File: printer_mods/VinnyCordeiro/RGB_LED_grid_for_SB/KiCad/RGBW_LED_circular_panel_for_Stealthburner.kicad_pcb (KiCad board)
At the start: 2 copper layers, 13.4 x 11.6 mm, 11 parts, among them J1 Conn_02x03_Odd_Even

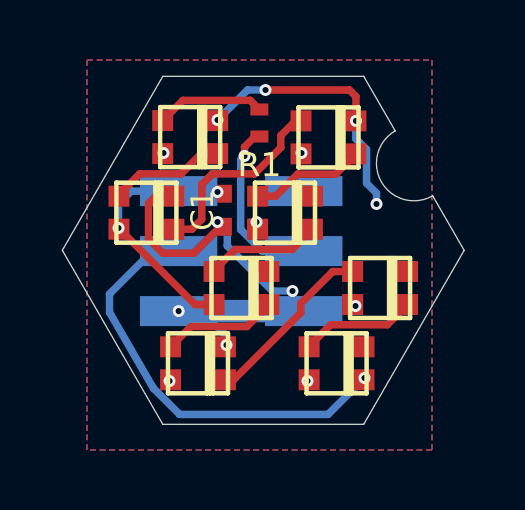
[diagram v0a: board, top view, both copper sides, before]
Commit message: Updated PCB, solve need for inline resistor for impedance matching (#716)
* Create README.md

* Create README.md

* Update README.md

* Added KiCad project files

* Create README.md

* Added production files

* Update README.md

Added note on mixing RGB and RGBW LEDs.

* Update README.md

typo

* Create README.md

* Update README.md

Added VinnyCordeiro's RGB LED grid for Stealthburner

* Add files via upload

Animated GIF of the board working

* Update README.md

* Update README.md

* Update README.md

Added the KiCad version that was used to design the PCB

* Removed non-necessary components

Removed both the input resistor and the filtering capacitor, as they are not strictly necessary for this application.

* Delete bom.csv

* Delete cpl.csv

* Delete RGBW_LED_circular_panel_for_Stealthburner.zip

* Updated production files

* Update README.md
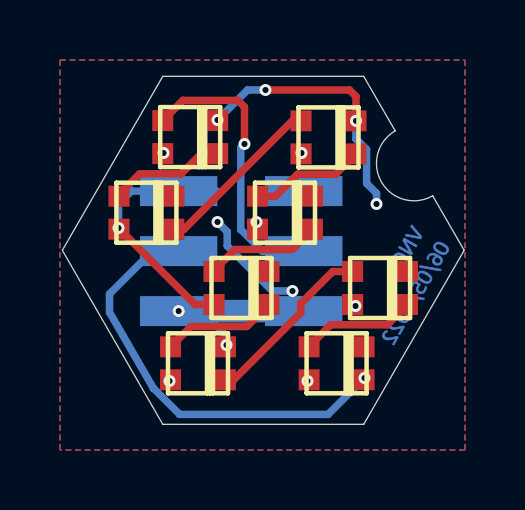
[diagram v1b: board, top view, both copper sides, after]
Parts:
- removed C1: 100nF, Capacitors_SMD:C_0402_NoSilk
- removed R1: 470R, Resistors_SMD:R_0402_NoSilk
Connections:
- D1 pad 4: Net-(D1-Pad4) -> LED_IN
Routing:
- net GND: track 25.2 -> 19.9 mm
- net LED_IN: track 5.84 -> 9.63 mm
- net Net-(D1-Pad4): track 3.63 -> 0.00 mm
- net R1_R2: track 6.65 -> 5.74 mm
- net +5V: track 9.12 -> 8.87 mm, vias 8 -> 7
